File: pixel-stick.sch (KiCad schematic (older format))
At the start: 12 parts, among them J1 WS2811, U1 AZ1117-3.3, U2 RT9361AGE, U3 MC74VHC1GT125

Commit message: make it tiny, based on simple blocks
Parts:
- removed C1: 100µF, Capacitor_SMD:CP_Elec_6.3x7.7, symbol Device:CP1
- removed F1: Polyfuse, Resistor_SMD:R_1206_3216Metric_Pad1.42x1.75mm_HandSolder, symbol Device:Polyfuse
- removed U1: AZ1117-3.3, Package_TO_SOT_SMD:SOT-223-3_TabPin2, symbol Regulator_Linear:AZ1117-3.3
- removed U3: MC74VHC1GT125, Package_TO_SOT_SMD:SOT-23-5_HandSoldering, symbol 74xGxx:74AHC1G125
- added 2.2uH1: L, Inductor_SMD:L_Taiyo-Yuden_MD-2020, symbol Device:L
- added C1: 10µF, Capacitor_SMD:C_0805_2012Metric, symbol Device:C
- added Q1: BSS138, Package_TO_SOT_SMD:SOT-23, symbol Transistor_FET:BSS138
- added R1, R2: 10k, Resistor_SMD:R_0805_2012Metric, symbol Device:R
- added U1: LM3670MF, Package_TO_SOT_SMD:TSOT-23-5, symbol Regulator_Switching:LM3670MF
- C2: value 1µF -> 10µF; footprint Capacitor_SMD:C_1206_3216Metric_Pad1.42x1.75mm_HandSolder -> Capacitor_SMD:C_0805_2012Metric
- C3: value 10µF -> 22µF; footprint Capacitor_SMD:C_1206_3216Metric_Pad1.42x1.75mm_HandSolder -> Capacitor_SMD:C_0805_2012Metric
- C4, C5, C6: footprint Capacitor_SMD:C_1206_3216Metric_Pad1.42x1.75mm_HandSolder -> Capacitor_SMD:C_0805_2012Metric
- J1: value WS2811 -> WS281*
- U2: footprint Package_TO_SOT_SMD:SOT-23-6_Handsoldering -> Package_TO_SOT_SMD:SOT-23-6
- renumbered ESP-01 to ESP-1
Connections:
- net labels added: +3V3
- net labels removed: +3.3V
- wire segments 56 -> 66
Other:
- note added: "3.3V Power Regulation"
- note added: "3.3V to 5V Level Shifting"
- note added: "5V Power Regulation"
- note added: "ESP8266 WiFi Controller"
- note removed: "Digital IO"
- note removed: "Power Management"
- note removed: "WiFi Microcontroller"
- moved on the sheet: C2, C3, C4, C5, C6, ESP-1

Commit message: fix library symbols
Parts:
- removed U2: RT9361AGE, Package_TO_SOT_SMD:SOT-23-6, symbol Regulator_Linear:AP3602A
- added U2: RT9361A, Package_TO_SOT_SMD:SOT-23-6, symbol pixel-stick:RT9361A
- ESP-1: footprint ESP8266:ESP-01 -> Connector_PinHeader_2.54mm:PinHeader_2x04_P2.54mm_Vertical
- J1: footprint Connector_Wire:SolderWirePad_1x03_P3.81mm_Drill1.2mm -> Connector_PinHeader_2.00mm:PinHeader_1x03_P2.00mm_Vertical
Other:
- moved on the sheet: C4, C6
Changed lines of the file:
@@
 EESchema Schematic File Version 4
 LIBS:pixel-stick-cache
-EELAYER 29 0
+EELAYER 30 0
 EELAYER END
 $Descr A4 11693 8268
@@
 3.3V Power Regulation
 $Comp
-L Regulator_Linear:AP3602A U2
-U 1 1 5DEB2EA3
-P 8100 1300
-F 0 "U2" H 8100 1300 50  0000 C CNN
-F 1 "RT9361AGE" H 8100 1200 50  0000 C CNN
-F 2 "Package_TO_SOT_SMD:SOT-23-6" H 8100 1233 50  0001 C CNN
-F 3 "https://www.richtek.com/assets/product_file/RT9361A=RT9361B/DS9361AB-14.pdf" H 8100 1300 50  0001 C CNN
-	1    8100 1300
-	1    0    0    -1
-$EndComp
-$Comp
 L power:GND #PWR08
 U 1 1 5DEBAE40
@@
 $EndComp
 Wire Wire Line
-	7600 1650 7500 1650
+	7650 1650 7500 1650
 Wire Wire Line
 	7500 1650 7500 1500
 Wire Wire Line
-	7500 1500 7600 1500
-Wire Wire Line
-	8600 1500 9200 1500
+	7500 1500 7650 1500
+Wire Wire Line
+	8550 1500 9200 1500
 Connection ~ 9200 1500
 Wire Wire Line
-	8600 1650 8750 1650
+	8550 1650 8750 1650
 Wire Wire Line
 	8750 1650 8750 2150
@@
 Text Notes 6300 5950 0    157  ~ 0
 3.3V to 5V Level Shifting
-Connection ~ 2800 4550
-Wire Wire Line
-	2800 4700 2800 4550
-Wire Wire Line
-	2900 4700 2800 4700
 Text Notes 1850 5950 0    157  ~ 0
 ESP8266 WiFi Controller
 Wire Wire Line
-	2800 4400 2800 4550
-Wire Wire Line
-	2050 4950 2050 5350
-Wire Wire Line
-	2050 4400 2050 4650
-Text Label 4500 4950 0    50   ~ 0
+	1850 4800 1850 5050
+Wire Wire Line
+	1850 4300 1850 4500
+Text Label 2600 4850 0    50   ~ 0
 RXD
-Text Label 4500 4800 0    50   ~ 0
+Text Label 2600 4700 0    50   ~ 0
 TXD
-Text Label 4500 4550 0    50   ~ 0
+Text Label 4550 4250 0    50   ~ 0
 GPIO0
-Text Label 4500 4400 0    50   ~ 0
+Text Label 4550 4400 0    50   ~ 0
 GPIO2
 Wire Wire Line
-	2900 4550 2800 4550
-Wire Wire Line
-	2900 4400 2800 4400
-Wire Wire Line
-	4400 4950 4750 4950
-Wire Wire Line
-	4400 4800 4750 4800
-Wire Wire Line
-	4400 4550 4750 4550
-Wire Wire Line
-	4400 4400 4750 4400
-Wire Wire Line
-	3650 5350 3650 5200
+	2500 4850 2850 4850
+Wire Wire Line
+	2500 4700 2850 4700
+Wire Wire Line
+	4450 4250 4800 4250
+Wire Wire Line
+	4450 4400 4800 4400
+Wire Wire Line
+	3650 5350 3650 5300
 $Comp
 L power:GND #PWR014
@@
 L power:GND #PWR013
 U 1 1 5DEA0257
-P 2050 5350
-F 0 "#PWR013" H 2050 5100 50  0001 C CNN
-F 1 "GND" H 2055 5177 50  0000 C CNN
-F 2 "" H 2050 5350 50  0001 C CNN
-F 3 "" H 2050 5350 50  0001 C CNN
-	1    2050 5350
+P 1850 5050
+F 0 "#PWR013" H 1850 4800 50  0001 C CNN
+F 1 "GND" H 1855 4877 50  0000 C CNN
+F 2 "" H 1850 5050 50  0001 C CNN
+F 3 "" H 1850 5050 50  0001 C CNN
+	1    1850 5050
 	1    0    0    -1
 $EndComp
@@
 L Device:C C6
 U 1 1 5DE9F007
-P 2050 4800
-F 0 "C6" H 2165 4846 50  0000 L CNN
-F 1 "10µF" H 2165 4755 50  0000 L CNN
-F 2 "Capacitor_SMD:C_0805_2012Metric" H 2088 4650 50  0001 C CNN
-F 3 "~" H 2050 4800 50  0001 C CNN
-	1    2050 4800
+P 1850 4650
+F 0 "C6" H 1965 4696 50  0000 L CNN
+F 1 "10µF" H 1965 4605 50  0000 L CNN
+F 2 "Capacitor_SMD:C_0805_2012Metric" H 1888 4500 50  0001 C CNN
+F 3 "~" H 1850 4650 50  0001 C CNN
+	1    1850 4650
 	1    0    0    -1
 $EndComp
@@
 F 0 "ESP-1" H 3650 5000 50  0000 C CNN
 F 1 "ESP-01v090" H 3650 4900 50  0000 C CNN
-F 2 "ESP8266:ESP-01" H 3650 4450 50  0001 C CNN
+F 2 "Connector_PinHeader_2.54mm:PinHeader_2x04_P2.54mm_Vertical" H 3650 4450 50  0001 C CNN
 F 3 "http://l0l.org.uk/2014/12/esp8266-modules-hardware-guide-gotta-catch-em-all/" H 3650 4450 50  0001 C CNN
 	1    3650 4450
@@
 $EndComp
 Wire Wire Line
-	7800 2150 7800 2000
-Wire Wire Line
-	8400 2000 8400 2150
-Wire Wire Line
-	7950 2150 7800 2150
-Wire Wire Line
-	8400 2150 8250 2150
+	7850 2200 7850 2050
+Wire Wire Line
+	8350 2050 8350 2200
+Wire Wire Line
+	7950 2200 7850 2200
+Wire Wire Line
+	8350 2200 8250 2200
 $Comp
 L Device:C C4
 U 1 1 5DEB5F38
-P 8100 2150
-F 0 "C4" V 7950 2150 50  0000 C CNN
-F 1 "1µF" V 8250 2150 50  0000 C CNN
-F 2 "Capacitor_SMD:C_0805_2012Metric" H 8138 2000 50  0001 C CNN
-F 3 "~" H 8100 2150 50  0001 C CNN
-	1    8100 2150
+P 8100 2200
+F 0 "C4" V 7950 2200 50  0000 C CNN
+F 1 "1µF" V 8250 2200 50  0000 C CNN
+F 2 "Capacitor_SMD:C_0805_2012Metric" H 8138 2050 50  0001 C CNN
+F 3 "~" H 8100 2200 50  0001 C CNN
+	1    8100 2200
 	0    1    1    0
 $EndComp
@@
 F 0 "J1" H 1980 1742 50  0000 L CNN
 F 1 "WS281*" H 1980 1651 50  0000 L CNN
-F 2 "Connector_Wire:SolderWirePad_1x03_P3.81mm_Drill1.2mm" H 1900 1700 50  0001 C CNN
+F 2 "Connector_PinHeader_2.00mm:PinHeader_1x03_P2.00mm_Vertical" H 1900 1700 50  0001 C CNN
 F 3 "~" H 1900 1700 50  0001 C CNN
 	1    1900 1700
@@
 Wire Wire Line
 	1250 1700 1700 1700
-$Comp
-L power:VIN #PWR0101
-U 1 1 5DFA6142
-P 1550 1500
-F 0 "#PWR0101" H 1550 1350 50  0001 C CNN
-F 1 "VIN" H 1565 1673 50  0000 C CNN
-F 2 "" H 1550 1500 50  0001 C CNN
-F 3 "" H 1550 1500 50  0001 C CNN
-	1    1550 1500
-	1    0    0    -1
-$EndComp
 $Comp
 L power:GND #PWR0102
@@
 Wire Wire Line
 	1550 1800 1700 1800
-$Comp
-L power:VIN #PWR0103
-U 1 1 5DFAB074
-P 3600 1350
-F 0 "#PWR0103" H 3600 1200 50  0001 C CNN
-F 1 "VIN" H 3615 1523 50  0000 C CNN
-F 2 "" H 3600 1350 50  0001 C CNN
-F 3 "" H 3600 1350 50  0001 C CNN
-	1    3600 1350
-	1    0    0    -1
-$EndComp
 Wire Wire Line
 	3600 1350 3600 1500
@@
 L power:+3V3 #PWR0111
 U 1 1 5E00CD04
-P 2050 4400
-F 0 "#PWR0111" H 2050 4250 50  0001 C CNN
-F 1 "+3V3" H 2065 4573 50  0000 C CNN
-F 2 "" H 2050 4400 50  0001 C CNN
-F 3 "" H 2050 4400 50  0001 C CNN
-	1    2050 4400
+P 1850 4300
+F 0 "#PWR0111" H 1850 4150 50  0001 C CNN
+F 1 "+3V3" H 1865 4473 50  0000 C CNN
+F 2 "" H 1850 4300 50  0001 C CNN
+F 3 "" H 1850 4300 50  0001 C CNN
+	1    1850 4300
 	1    0    0    -1
 $EndComp
@@
 L power:+3V3 #PWR0112
 U 1 1 5E00FB7E
-P 2800 4400
-F 0 "#PWR0112" H 2800 4250 50  0001 C CNN
-F 1 "+3V3" H 2815 4573 50  0000 C CNN
-F 2 "" H 2800 4400 50  0001 C CNN
-F 3 "" H 2800 4400 50  0001 C CNN
-	1    2800 4400
-	1    0    0    -1
-$EndComp
-Connection ~ 2800 4400
+P 2700 4250
+F 0 "#PWR0112" H 2700 4100 50  0001 C CNN
+F 1 "+3V3" H 2715 4423 50  0000 C CNN
+F 2 "" H 2700 4250 50  0001 C CNN
+F 3 "" H 2700 4250 50  0001 C CNN
+	1    2700 4250
+	0    -1   -1   0
+$EndComp
 $Comp
 L Device:R R2
@@
 	1    0    0    -1
 $EndComp
+$Comp
+L power:+3V3 #PWR0101
+U 1 1 5DF8D87E
+P 4600 4700
+F 0 "#PWR0101" H 4600 4550 50  0001 C CNN
+F 1 "+3V3" H 4615 4873 50  0000 C CNN
+F 2 "" H 4600 4700 50  0001 C CNN
+F 3 "" H 4600 4700 50  0001 C CNN
+	1    4600 4700
+	0    1    1    0
+$EndComp
+Wire Wire Line
+	4600 4700 4450 4700
+Wire Wire Line
+	2850 4250 2800 4250
+Wire Wire Line
+	2850 4400 2800 4400
+Wire Wire Line
+	2800 4400 2800 4250
+Connection ~ 2800 4250
+Wire Wire Line
+	2800 4250 2700 4250
+$Comp
+L pixel-stick:RT9361A U2
+U 1 1 5DF9FB9E
+P 8100 1250
+F 0 "U2" H 8100 1242 50  0000 C CNN
+F 1 "RT9361A" H 8100 1151 50  0000 C CNN
+F 2 "Package_TO_SOT_SMD:SOT-23-6" H 8100 1250 50  0001 C CNN
+F 3 "https://media.digikey.com/pdf/Data%20Sheets/Diodes%20PDFs/AP3602A_B.pdf" H 8100 1250 50  0001 C CNN
+	1    8100 1250
+	1    0    0    -1
+$EndComp
+$Comp
+L pixel-stick:VIN #PWR0103
+U 1 1 5DFABE49
+P 3600 1350
+F 0 "#PWR0103" H 3600 1200 50  0001 C CNN
+F 1 "VIN" H 3615 1523 50  0000 C CNN
+F 2 "" H 3600 1350 50  0001 C CNN
+F 3 "" H 3600 1350 50  0001 C CNN
+	1    3600 1350
+	1    0    0    -1
+$EndComp
+$Comp
+L pixel-stick:VIN #PWR0113
+U 1 1 5DFAC466
+P 1550 1500
+F 0 "#PWR0113" H 1550 1350 50  0001 C CNN
+F 1 "VIN" H 1565 1673 50  0000 C CNN
+F 2 "" H 1550 1500 50  0001 C CNN
+F 3 "" H 1550 1500 50  0001 C CNN
+	1    1550 1500
+	1    0    0    -1
+$EndComp

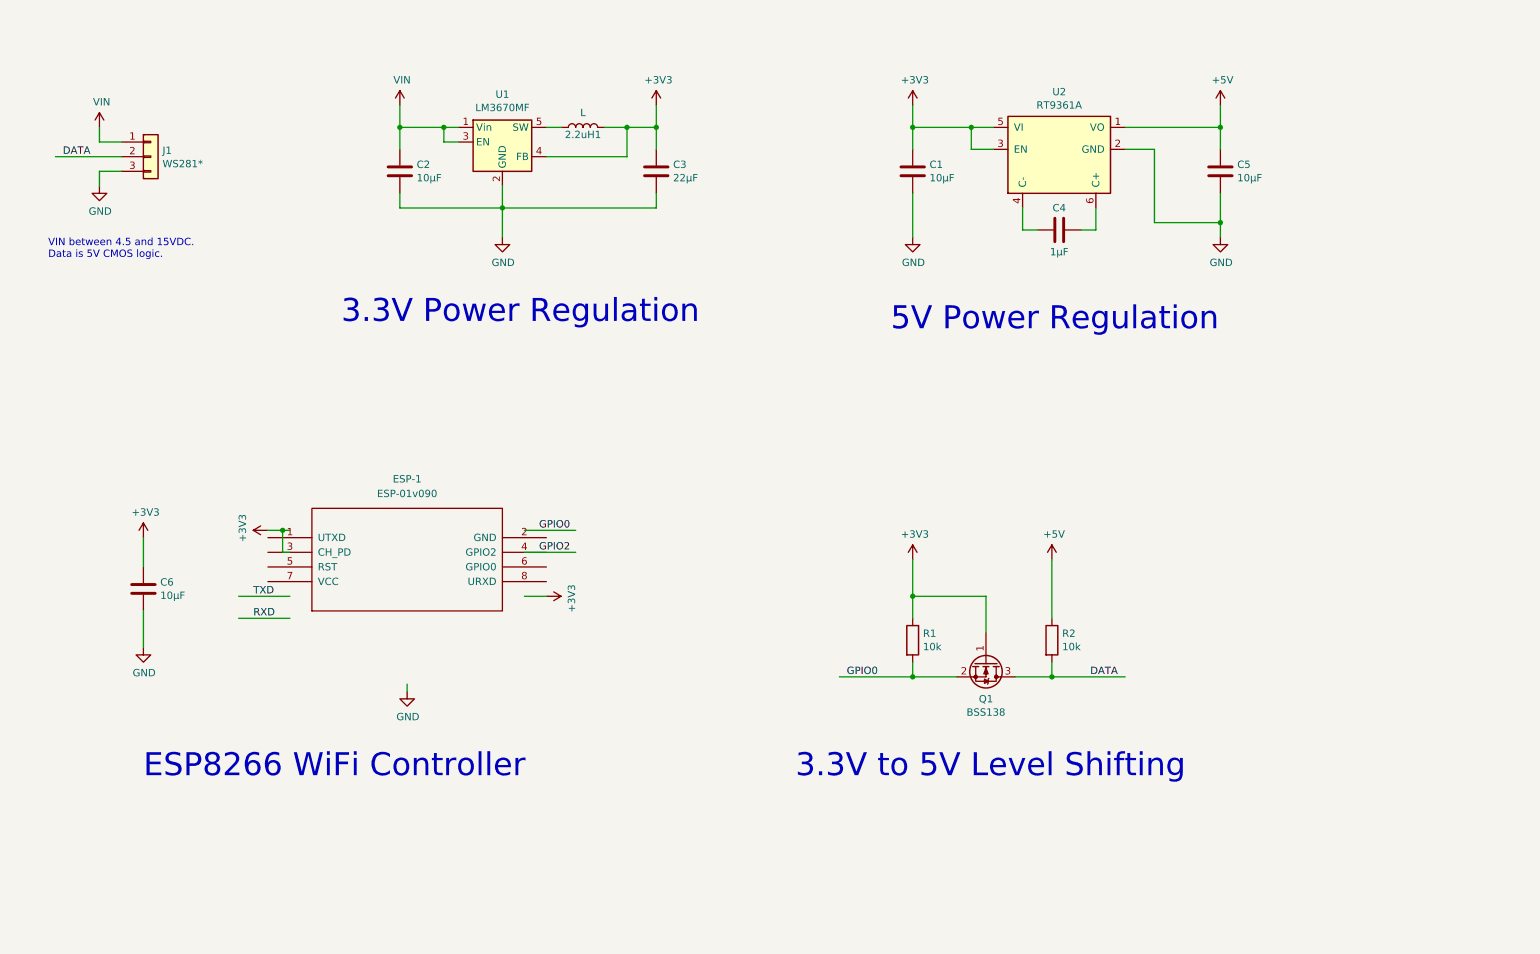
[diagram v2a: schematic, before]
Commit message: add esp module
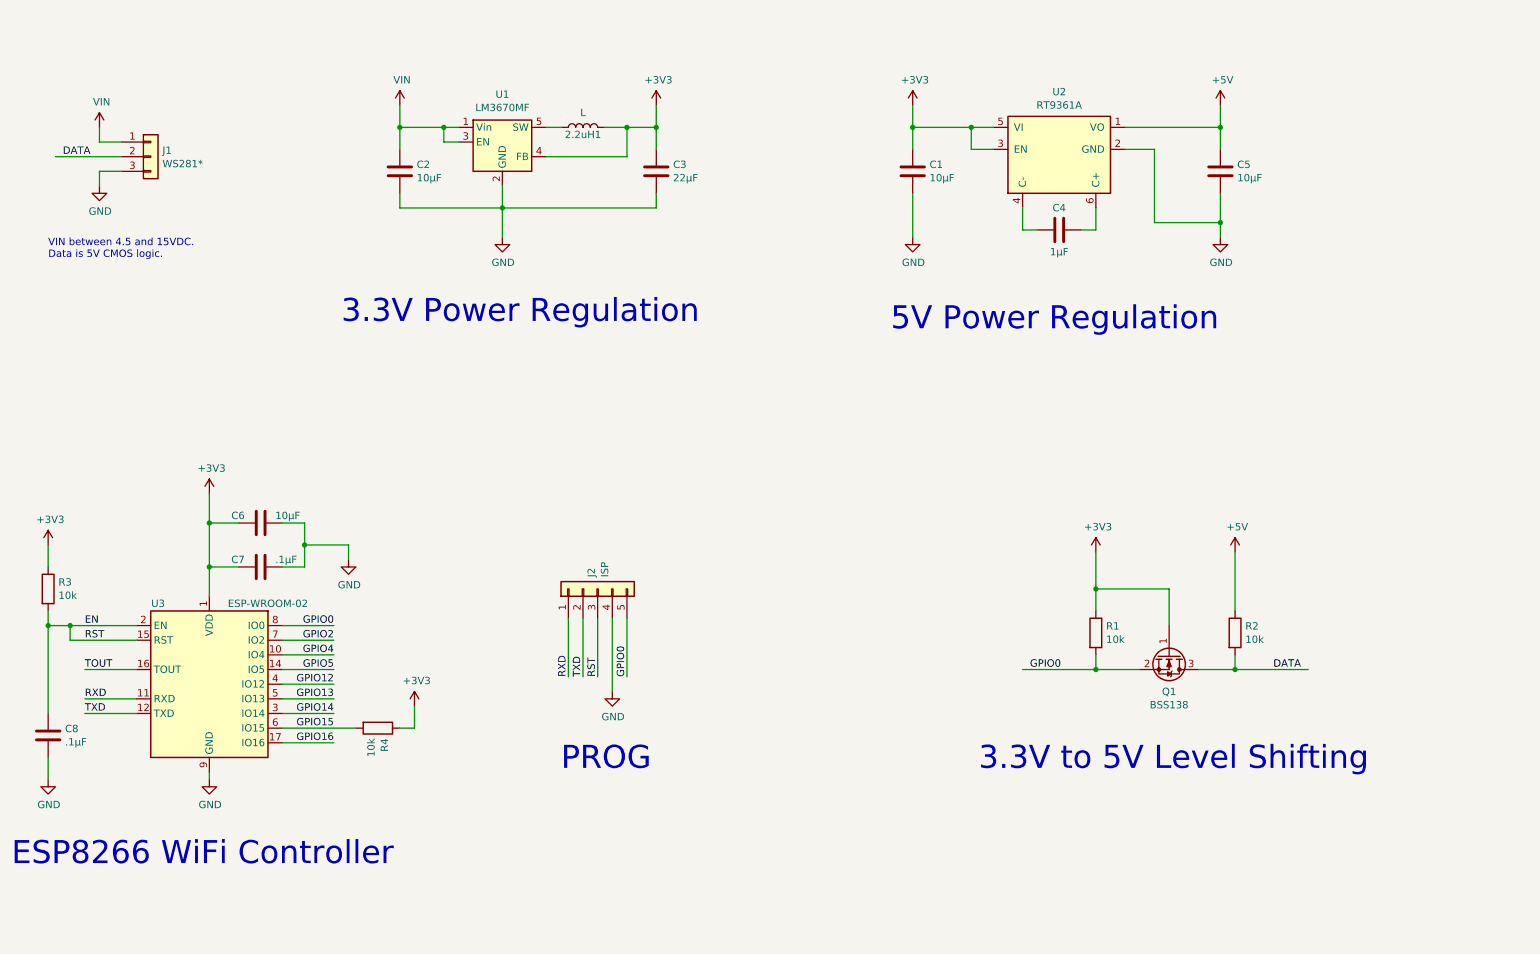
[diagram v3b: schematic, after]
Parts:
- removed ESP-1: ESP-01v090, Connector_PinHeader_2.54mm:PinHeader_2x04_P2.54mm_Vertical, symbol ESP8266:ESP-01v090
- added C7, C8: .1µF, Capacitor_SMD:C_0805_2012Metric, symbol Device:C
- added J2: ISP, Connector_PinHeader_2.00mm:PinHeader_1x05_P2.00mm_Vertical, symbol Connector_Generic:Conn_01x05
- added R3, R4: 10k, Resistor_SMD:R_0805_2012Metric, symbol Device:R
- added U3: ESP-WROOM-02, RF_Module:ESP-WROOM-02, symbol RF_Module:ESP-WROOM-02
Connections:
- net labels added: EN, GPIO12, GPIO13, GPIO14, GPIO15, GPIO16, GPIO4, GPIO5, RST, TOUT
- wire segments 66 -> 93
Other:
- note added: "PROG"
- moved on the sheet: C6, Q1, R1, R2

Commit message: layout board with ESP-M2
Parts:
- removed C7, C8: .1µF, Capacitor_SMD:C_0805_2012Metric, symbol Device:C
- removed R4: 10k, Resistor_SMD:R_0805_2012Metric, symbol Device:R
- removed U3: ESP-WROOM-02, RF_Module:ESP-WROOM-02, symbol RF_Module:ESP-WROOM-02
- added SW1: RESET, Button_Switch_SMD:SW_Push_SPST_NO_Alps_SKRK, symbol Switch:SW_SPST
- added SW2: PROG, Button_Switch_SMD:SW_Push_SPST_NO_Alps_SKRK, symbol Switch:SW_SPST
- added U4: ESP-M2, ESP8285:ESP-M2, symbol ESP8285:ESP-M2
- C6: value 10µF -> 22µF
- J1: footprint Connector_PinHeader_2.00mm:PinHeader_1x03_P2.00mm_Vertical -> Connector_PinHeader_2.54mm:PinHeader_1x03_P2.54mm_Vertical
- J2: footprint Connector_PinHeader_2.00mm:PinHeader_1x05_P2.00mm_Vertical -> Connector_PinHeader_2.54mm:PinHeader_1x02_P2.54mm_Vertical; symbol Connector_Generic:Conn_01x05 -> Connector_Generic:Conn_01x02
- L1: renamed from 2.2uH1; value L -> 2.2uH
- U1: footprint Package_TO_SOT_SMD:TSOT-23-5 -> Package_TO_SOT_SMD:SOT-23-5
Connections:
- net labels removed: EN, GPIO12, GPIO13, GPIO14, GPIO15, GPIO16, GPIO2, GPIO4, GPIO5, TOUT
- wire segments 93 -> 74
- no-connect marks 0 -> 8
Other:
- note removed: "PROG"

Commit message: use jst-ph connector
populating the connector is optional, the pads can be used for either direct solder wires or for a jst-ph to jst-sm adapter
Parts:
- J1: footprint Connector_PinHeader_2.54mm:PinHeader_1x03_P2.54mm_Vertical -> Connector_JST:JST_PH_S3B-PH-K_1x03_P2.00mm_Horizontal
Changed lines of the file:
@@
 EESchema Schematic File Version 4
 LIBS:pixel-stick-cache
-EELAYER 29 0
+EELAYER 30 0
 EELAYER END
 $Descr A4 11693 8268
@@
 F 0 "J1" H 1980 1742 50  0000 L CNN
 F 1 "WS281*" H 1980 1651 50  0000 L CNN
-F 2 "Connector_PinHeader_2.54mm:PinHeader_1x03_P2.54mm_Vertical" H 1900 1700 50  0001 C CNN
+F 2 "Connector_JST:JST_PH_S3B-PH-K_1x03_P2.00mm_Horizontal" H 1900 1700 50  0001 C CNN
 F 3 "~" H 1900 1700 50  0001 C CNN
 	1    1900 1700
